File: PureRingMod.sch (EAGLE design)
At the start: 36 parts, among them IC1 TL074P, IC2 TL072P, X1 NC3FD-V

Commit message: added mix control
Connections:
- net GND: now also MICVOL.1, R4.2
- net N$30: no longer R4.2
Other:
- moved on the sheet: R4
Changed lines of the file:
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@@
 <instance part="R2" gate="G$1" x="99.06" y="66.04"/>
 <instance part="R3" gate="G$1" x="-5.08" y="38.1"/>
-<instance part="R4" gate="G$1" x="-5.08" y="66.04"/>
+<instance part="R4" gate="G$1" x="-12.7" y="66.04"/>
 <instance part="R5" gate="G$1" x="132.08" y="63.5"/>
 <instance part="OUTPUT" gate="G$1" x="157.48" y="63.5"/>
@@
 <label x="-35.56" y="88.9" size="1.778" layer="95"/>
 </segment>
+<segment>
+<pinref part="MICVOL" gate="G$1" pin="1"/>
+<pinref part="R4" gate="G$1" pin="2"/>
+<wire x1="-7.62" y1="66.04" x2="-2.54" y2="66.04" width="0.1524" layer="91"/>
+<wire x1="-2.54" y1="66.04" x2="-2.54" y2="83.82" width="0.1524" layer="91"/>
+</segment>
 </net>
 <net name="-12V" class="1">
@@
 <wire x1="121.92" y1="63.5" x2="127" y2="63.5" width="0.1524" layer="91"/>
 <pinref part="R5" gate="G$1" pin="1"/>
-</segment>
-</net>
-<net name="N$13" class="0">
-<segment>
-<pinref part="R4" gate="G$1" pin="1"/>
-<wire x1="-10.16" y1="66.04" x2="-12.7" y2="66.04" width="0.1524" layer="91"/>
-<pinref part="CARRIERAC" gate="G$1" pin="P"/>
-<wire x1="-20.32" y1="66.04" x2="-12.7" y2="66.04" width="0.1524" layer="91"/>
 </segment>
 </net>
@@
 <pinref part="IC1" gate="A" pin="+IN"/>
 <wire x1="7.62" y1="66.04" x2="5.08" y2="66.04" width="0.1524" layer="91"/>
-<pinref part="R4" gate="G$1" pin="2"/>
 <wire x1="5.08" y1="66.04" x2="2.54" y2="66.04" width="0.1524" layer="91"/>
-<wire x1="2.54" y1="66.04" x2="0" y2="66.04" width="0.1524" layer="91"/>
 <wire x1="5.08" y1="88.9" x2="5.08" y2="66.04" width="0.1524" layer="91"/>
 <junction x="5.08" y="66.04"/>
 </segment>
 </net>
+<net name="N$8" class="0">
+<segment>
+<pinref part="CARRIERAC" gate="G$1" pin="P"/>
+<pinref part="R4" gate="G$1" pin="1"/>
+<wire x1="-20.32" y1="66.04" x2="-17.78" y2="66.04" width="0.1524" layer="91"/>
+</segment>
+</net>

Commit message: updated components in feedback circuit of preamp
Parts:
- R12: value 301K -> 330K
- TR1: value 25K -> 10K
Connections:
- net GND: now also OUTPUT.NORM
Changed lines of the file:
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@@
 <part name="R11" library="SparkFun-Resistors" deviceset="330OHM" device="-HORIZ-1/10W-5%" value="316K"/>
 <part name="C5" library="SparkFun-Capacitors" deviceset="0.1UF" device="-KIT-EZ-50V-20%" value="4u7f"/>
-<part name="R12" library="SparkFun-Resistors" deviceset="330OHM" device="-HORIZ-1/10W-5%" value="301K"/>
+<part name="R12" library="SparkFun-Resistors" deviceset="330OHM" device="-HORIZ-1/10W-5%" value="330K"/>
 <part name="R13" library="SparkFun-Resistors" deviceset="330OHM" device="-HORIZ-1/10W-5%" value="10K"/>
 <part name="R14" library="SparkFun-Resistors" deviceset="330OHM" device="-HORIZ-1/10W-5%" value="100"/>
-<part name="TR1" library="INSTRUO" deviceset="TRIMMER_TH3" device="" value="25K"/>
+<part name="TR1" library="INSTRUO" deviceset="TRIMMER_TH3" device="" value="10K"/>
 <part name="MICVOL" library="GMSN" deviceset="9MMPOT" device=""/>
 </parts>
@@
 <wire x1="149.86" y1="60.96" x2="149.86" y2="58.42" width="0.1524" layer="91"/>
 <label x="149.86" y="55.88" size="1.778" layer="95"/>
+<pinref part="OUTPUT" gate="G$1" pin="NORM"/>
+<wire x1="152.4" y1="63.5" x2="149.86" y2="63.5" width="0.1524" layer="91"/>
+<wire x1="149.86" y1="63.5" x2="149.86" y2="60.96" width="0.1524" layer="91"/>
+<junction x="149.86" y="60.96"/>
 </segment>
 <segment>

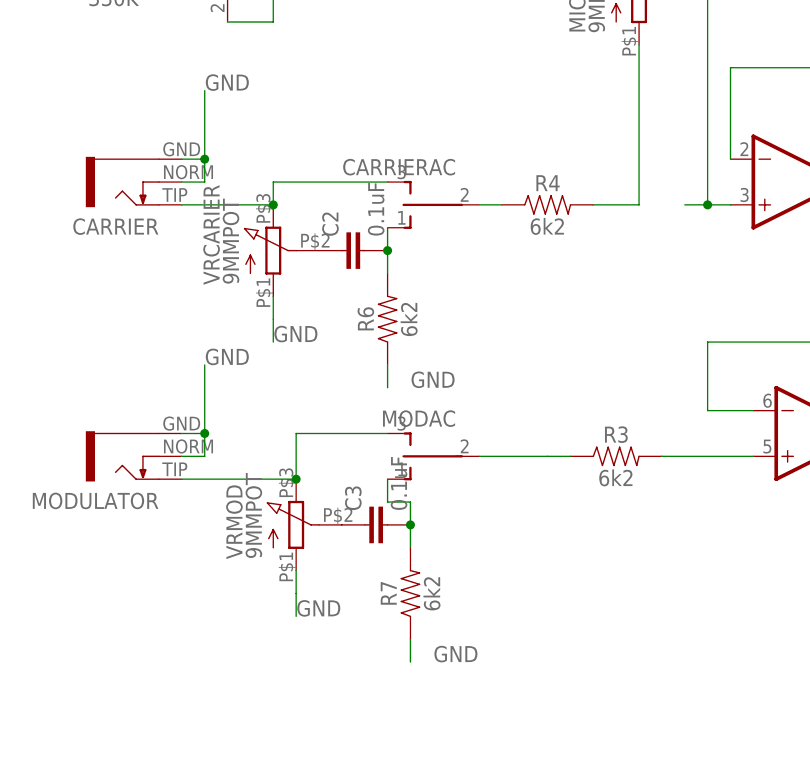
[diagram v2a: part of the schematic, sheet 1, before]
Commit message: Corrected values on input circuit
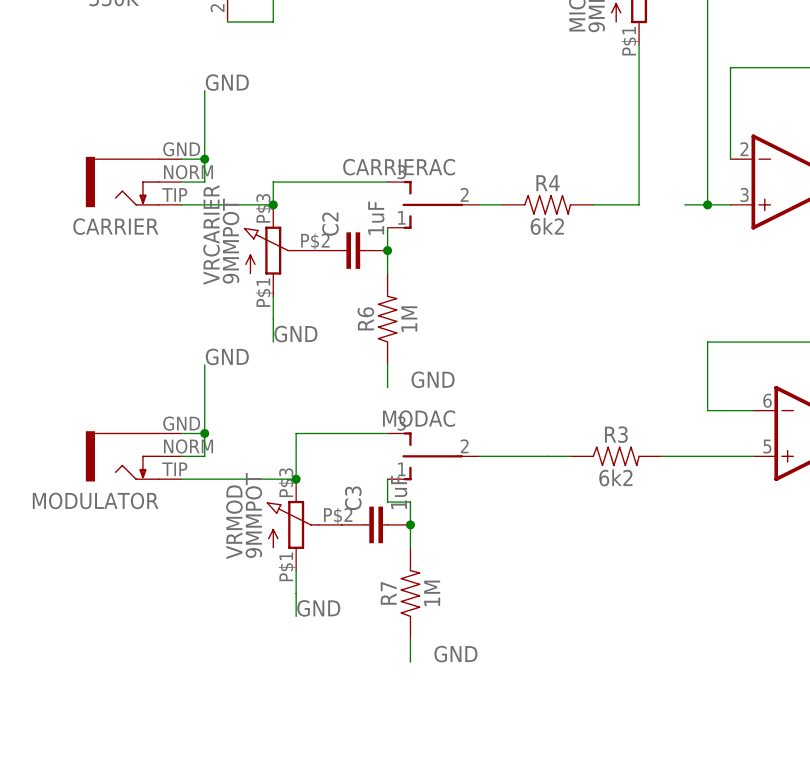
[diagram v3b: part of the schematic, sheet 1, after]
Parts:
- C2, C3: value 0.1uF -> 1uF
- R6, R7: value 6k2 -> 1M
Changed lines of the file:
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@@
 <part name="VRCARIER" library="GMSN" deviceset="9MMPOT" device=""/>
 <part name="VRMOD" library="GMSN" deviceset="9MMPOT" device=""/>
-<part name="C2" library="SparkFun-Capacitors" deviceset="0.1UF" device="-KIT-EZ-50V-20%" value="0.1uF"/>
-<part name="C3" library="SparkFun-Capacitors" deviceset="0.1UF" device="-KIT-EZ-50V-20%" value="0.1uF"/>
-<part name="R6" library="SparkFun-Resistors" deviceset="330OHM" device="-HORIZ-1/10W-5%" value="6k2"/>
-<part name="R7" library="SparkFun-Resistors" deviceset="330OHM" device="-HORIZ-1/10W-5%" value="6k2"/>
+<part name="C2" library="SparkFun-Capacitors" deviceset="0.1UF" device="-KIT-EZ-50V-20%" value="1uF"/>
+<part name="C3" library="SparkFun-Capacitors" deviceset="0.1UF" device="-KIT-EZ-50V-20%" value="1uF"/>
+<part name="R6" library="SparkFun-Resistors" deviceset="330OHM" device="-HORIZ-1/10W-5%" value="1M"/>
+<part name="R7" library="SparkFun-Resistors" deviceset="330OHM" device="-HORIZ-1/10W-5%" value="1M"/>
 <part name="X1" library="con-neutrik_ag" library_urn="urn:adsk.eagle:library:166" deviceset="NC3" device="FD-V" package3d_urn="urn:adsk.eagle:package:8819/1">
 <attribute name="RS-PART" value="448-244"/>

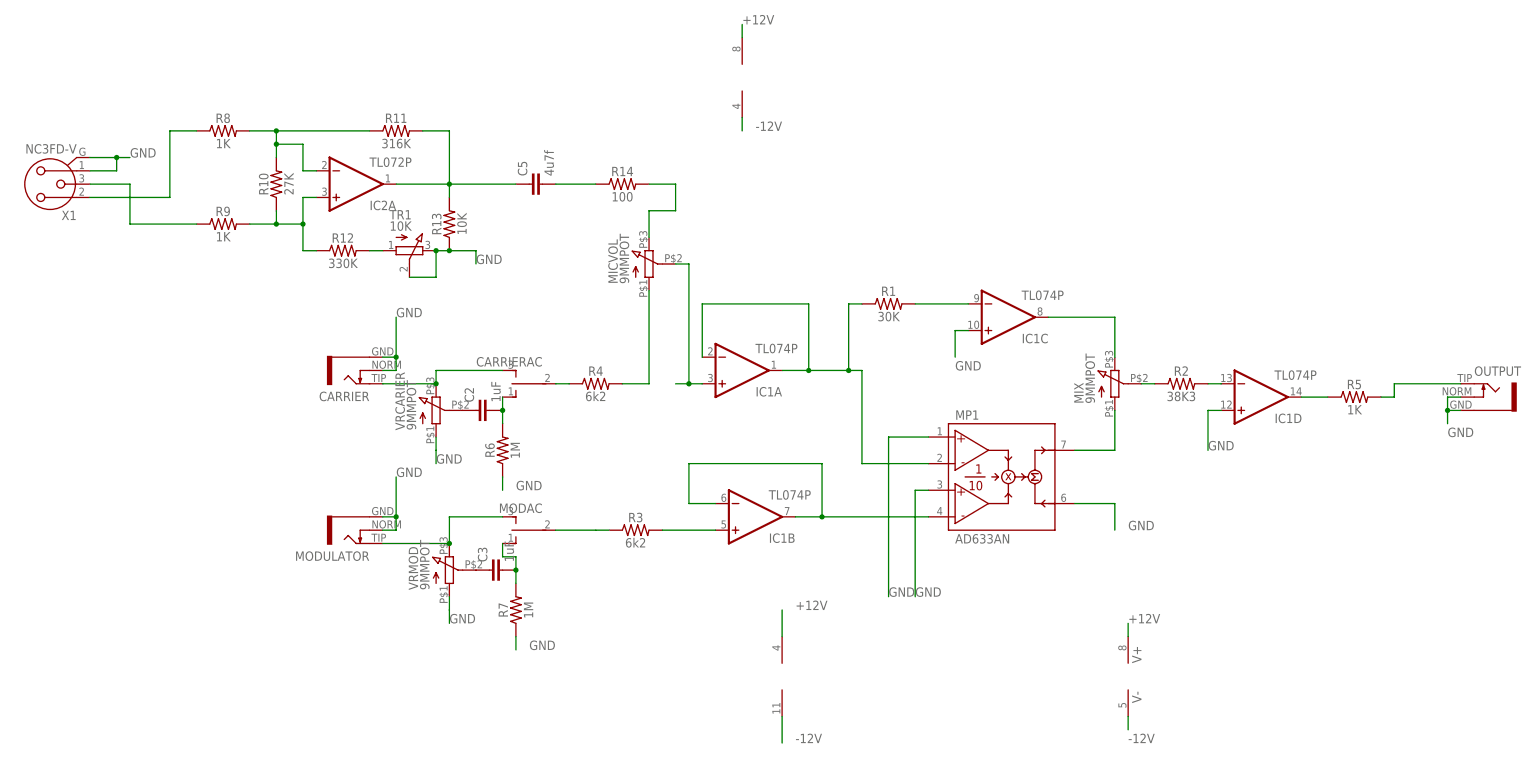
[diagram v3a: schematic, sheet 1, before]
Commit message: corrected input components
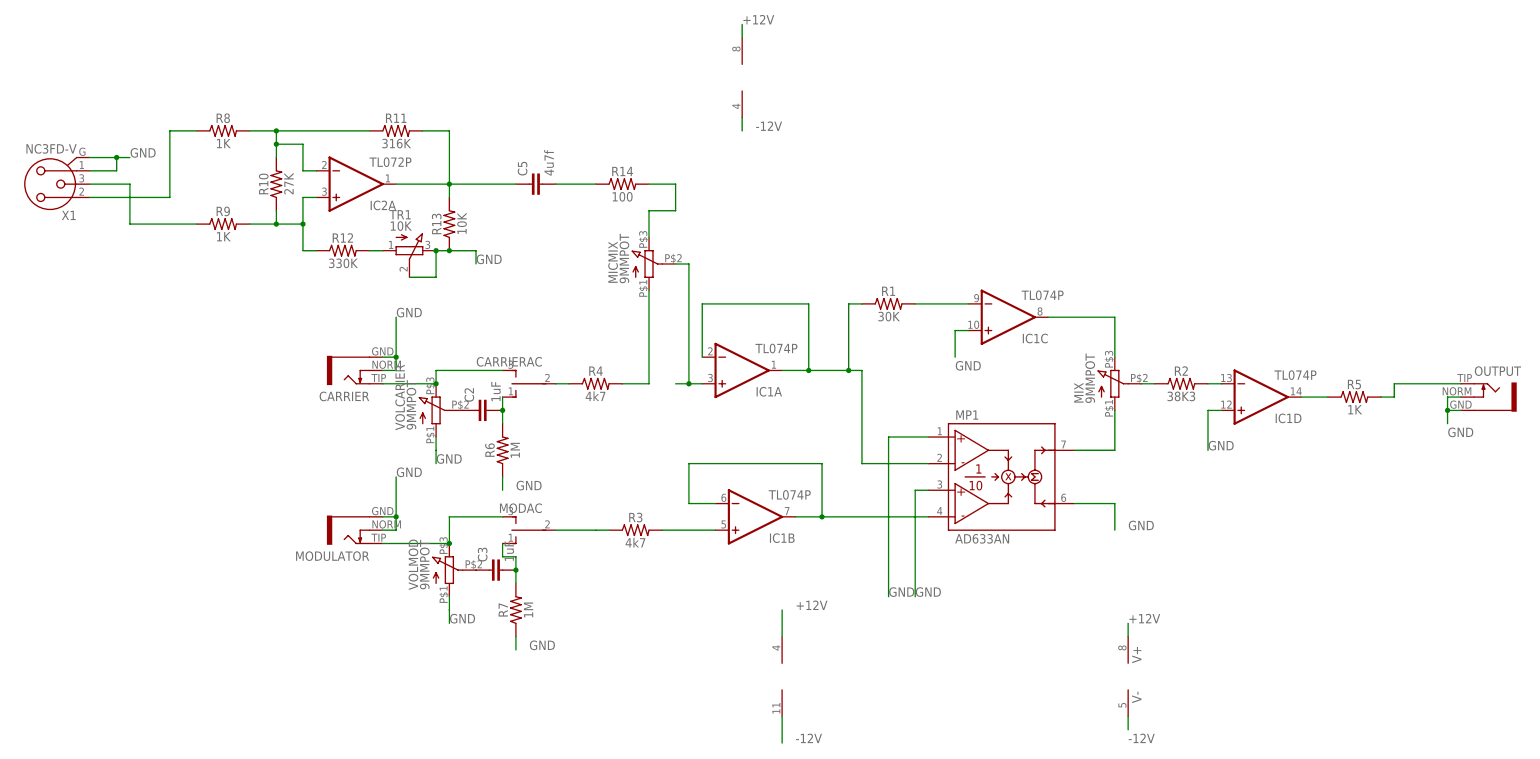
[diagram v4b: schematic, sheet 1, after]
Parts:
- R3, R4: value 6k2 -> 4k7
- renumbered MICVOL to MICMIX, VRCARIER to VOLCARIER, VRMOD to VOLMOD

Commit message: added missing parts
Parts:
- added R15: 10K, SparkFun-Resistors:330OHM-HORIZ-1/10W-5%
- added R16: 27K, SparkFun-Resistors:330OHM-HORIZ-1/10W-5%
- R1: value 30K -> 20K
- R2: value 38K3 -> 27K
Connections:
- net N$12: now also R16.2
- net N$4: now also R15.2
- net N$5: now also R15.1
- net N$7: now also R16.1
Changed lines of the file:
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@@
 <part name="POWER" library="SparkFun-Connectors" deviceset="M05X2" device="SHD"/>
 <part name="MIX" library="GMSN" deviceset="9MMPOT" device=""/>
-<part name="R1" library="SparkFun-Resistors" deviceset="330OHM" device="-HORIZ-1/10W-5%" value="30K"/>
-<part name="R2" library="SparkFun-Resistors" deviceset="330OHM" device="-HORIZ-1/10W-5%" value="38K3"/>
+<part name="R1" library="SparkFun-Resistors" deviceset="330OHM" device="-HORIZ-1/10W-5%" value="20K"/>
+<part name="R2" library="SparkFun-Resistors" deviceset="330OHM" device="-HORIZ-1/10W-5%" value="27K"/>
 <part name="C4" library="SparkFun-Capacitors" deviceset="10UF-POLAR" device="-RADIAL-2.5MM-25V-20%" value="10uF"/>
 <part name="C1" library="SparkFun-Capacitors" deviceset="10UF-POLAR" device="-RADIAL-2.5MM-25V-20%" value="10uF"/>
@@
 <part name="TR1" library="INSTRUO" deviceset="TRIMMER_TH3" device="" value="10K"/>
 <part name="MICMIX" library="GMSN" deviceset="9MMPOT" device=""/>
+<part name="R15" library="SparkFun-Resistors" deviceset="330OHM" device="-HORIZ-1/10W-5%" value="10K"/>
+<part name="R16" library="SparkFun-Resistors" deviceset="330OHM" device="-HORIZ-1/10W-5%" value="27K"/>
 </parts>
 <sheets>
@@
 </instance>
 <instance part="IC2" gate="P" x="15.24" y="124.46"/>
+<instance part="R15" gate="G$1" x="68.58" y="91.44">
+<attribute name="NAME" x="68.58" y="92.964" size="1.778" layer="95" font="vector" align="bottom-center"/>
+<attribute name="VALUE" x="68.58" y="89.916" size="1.778" layer="96" font="vector" align="top-center"/>
+</instance>
+<instance part="R16" gate="G$1" x="114.3" y="78.74">
+<attribute name="NAME" x="114.3" y="80.264" size="1.778" layer="95" font="vector" align="bottom-center"/>
+<attribute name="VALUE" x="114.3" y="77.216" size="1.778" layer="96" font="vector" align="top-center"/>
+</instance>
 </instances>
 <busses>
@@
 <segment>
 <pinref part="IC1" gate="C" pin="OUT"/>
-<wire x1="73.66" y1="78.74" x2="86.36" y2="78.74" width="0.1524" layer="91"/>
+<wire x1="73.66" y1="78.74" x2="78.74" y2="78.74" width="0.1524" layer="91"/>
 <pinref part="MIX" gate="G$1" pin="3"/>
+<wire x1="78.74" y1="78.74" x2="86.36" y2="78.74" width="0.1524" layer="91"/>
 <wire x1="86.36" y1="78.74" x2="86.36" y2="71.12" width="0.1524" layer="91"/>
+<wire x1="78.74" y1="78.74" x2="78.74" y2="91.44" width="0.1524" layer="91"/>
+<wire x1="78.74" y1="91.44" x2="73.66" y2="91.44" width="0.1524" layer="91"/>
+<pinref part="R15" gate="G$1" pin="2"/>
 </segment>
 </net>
@@
 <pinref part="R1" gate="G$1" pin="2"/>
 <pinref part="IC1" gate="C" pin="-IN"/>
-<wire x1="48.26" y1="81.28" x2="58.42" y2="81.28" width="0.1524" layer="91"/>
+<wire x1="48.26" y1="81.28" x2="53.34" y2="81.28" width="0.1524" layer="91"/>
+<wire x1="53.34" y1="81.28" x2="58.42" y2="81.28" width="0.1524" layer="91"/>
+<wire x1="53.34" y1="91.44" x2="53.34" y2="81.28" width="0.1524" layer="91"/>
+<junction x="53.34" y="81.28"/>
+<wire x1="53.34" y1="91.44" x2="63.5" y2="91.44" width="0.1524" layer="91"/>
+<pinref part="R15" gate="G$1" pin="1"/>
 </segment>
 </net>
@@
 <pinref part="IC1" gate="D" pin="-IN"/>
 <wire x1="104.14" y1="66.04" x2="106.68" y2="66.04" width="0.1524" layer="91"/>
+<wire x1="104.14" y1="66.04" x2="104.14" y2="78.74" width="0.1524" layer="91"/>
+<junction x="104.14" y="66.04"/>
+<pinref part="R16" gate="G$1" pin="1"/>
+<wire x1="104.14" y1="78.74" x2="109.22" y2="78.74" width="0.1524" layer="91"/>
 </segment>
 </net>
@@
 <segment>
 <pinref part="IC1" gate="D" pin="OUT"/>
-<wire x1="121.92" y1="63.5" x2="127" y2="63.5" width="0.1524" layer="91"/>
+<wire x1="121.92" y1="63.5" x2="124.46" y2="63.5" width="0.1524" layer="91"/>
 <pinref part="R5" gate="G$1" pin="1"/>
-</segment>
-</net>
+<wire x1="124.46" y1="63.5" x2="127" y2="63.5" width="0.1524" layer="91"/>
+<wire x1="124.46" y1="63.5" x2="124.46" y2="78.74" width="0.1524" layer="91"/>
+<junction x="124.46" y="63.5"/>
+<pinref part="R16" gate="G$1" pin="2"/>
+<wire x1="119.38" y1="78.74" x2="124.46" y2="78.74" width="0.1524" layer="91"/>
+</segment>
+</net>

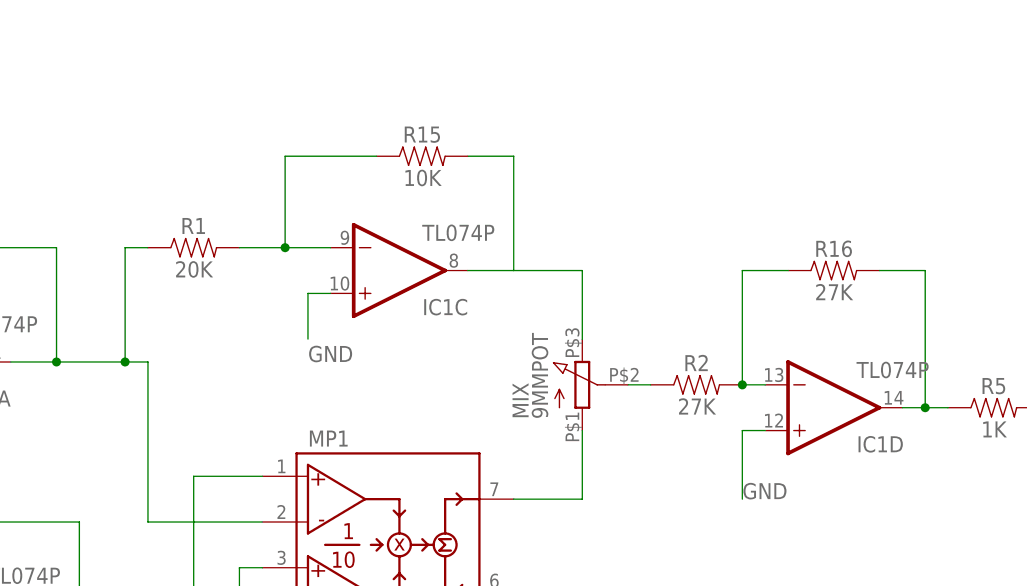
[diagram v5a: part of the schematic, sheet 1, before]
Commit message: Changed output circuit values
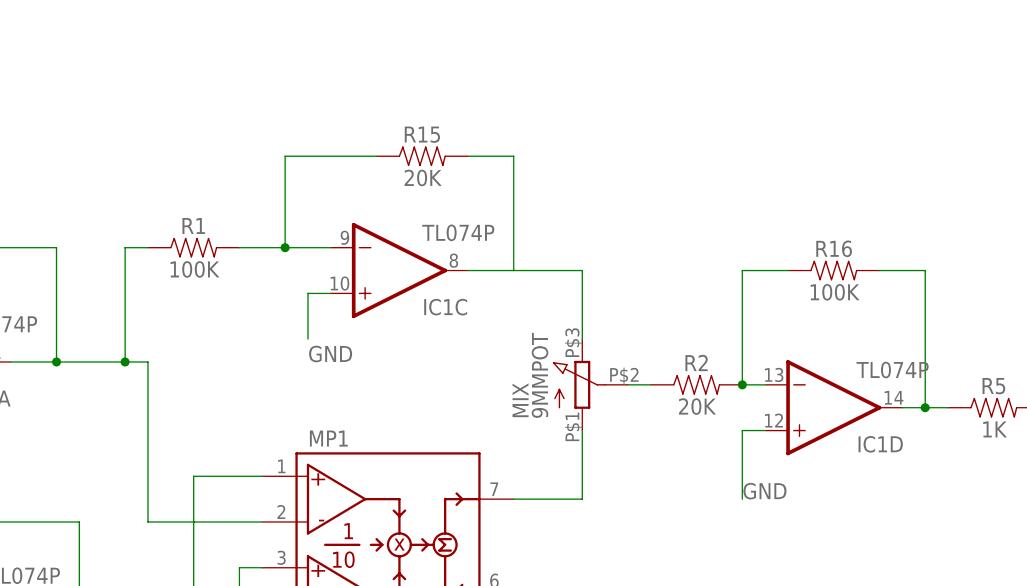
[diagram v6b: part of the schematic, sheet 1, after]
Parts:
- R1: value 20K -> 100K
- R15: value 10K -> 20K
- R16: value 27K -> 100K
- R2: value 27K -> 20K
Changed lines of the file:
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@@
 <part name="POWER" library="SparkFun-Connectors" deviceset="M05X2" device="SHD"/>
 <part name="MIX" library="GMSN" deviceset="9MMPOT" device=""/>
-<part name="R1" library="SparkFun-Resistors" deviceset="330OHM" device="-HORIZ-1/10W-5%" value="20K"/>
-<part name="R2" library="SparkFun-Resistors" deviceset="330OHM" device="-HORIZ-1/10W-5%" value="27K"/>
+<part name="R1" library="SparkFun-Resistors" deviceset="330OHM" device="-HORIZ-1/10W-5%" value="100K"/>
+<part name="R2" library="SparkFun-Resistors" deviceset="330OHM" device="-HORIZ-1/10W-5%" value="20K"/>
 <part name="C4" library="SparkFun-Capacitors" deviceset="10UF-POLAR" device="-RADIAL-2.5MM-25V-20%" value="10uF"/>
 <part name="C1" library="SparkFun-Capacitors" deviceset="10UF-POLAR" device="-RADIAL-2.5MM-25V-20%" value="10uF"/>
@@
 <part name="TR1" library="INSTRUO" deviceset="TRIMMER_TH3" device="" value="10K"/>
 <part name="MICMIX" library="GMSN" deviceset="9MMPOT" device=""/>
-<part name="R15" library="SparkFun-Resistors" deviceset="330OHM" device="-HORIZ-1/10W-5%" value="10K"/>
-<part name="R16" library="SparkFun-Resistors" deviceset="330OHM" device="-HORIZ-1/10W-5%" value="27K"/>
+<part name="R15" library="SparkFun-Resistors" deviceset="330OHM" device="-HORIZ-1/10W-5%" value="20K"/>
+<part name="R16" library="SparkFun-Resistors" deviceset="330OHM" device="-HORIZ-1/10W-5%" value="100K"/>
 </parts>
 <sheets>

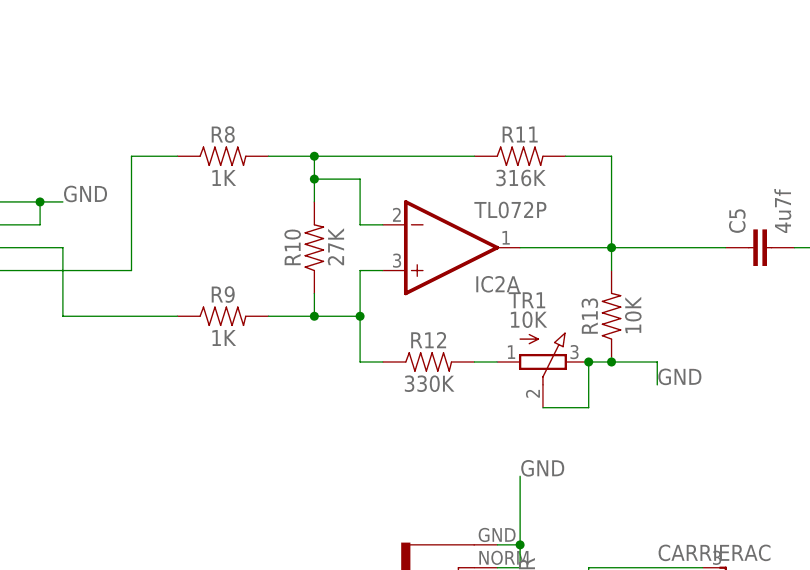
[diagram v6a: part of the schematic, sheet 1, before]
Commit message: modified input mic circuit
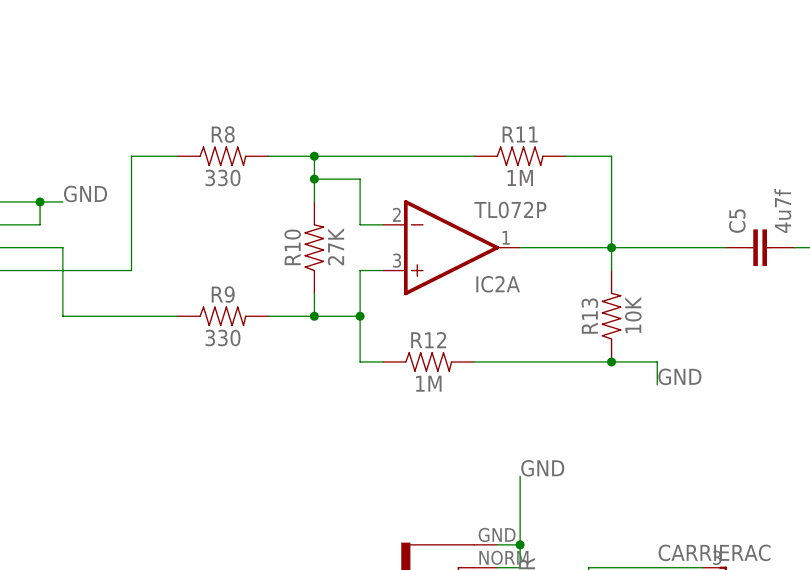
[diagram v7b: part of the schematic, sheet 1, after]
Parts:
- removed TR1: 10K, INSTRUO:TRIMMER_TH3
- R11: value 316K -> 1M
- R12: value 330K -> 1M
- R8, R9: value 1K -> 330
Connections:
- removed net N$28: R12.2, TR1.1
- net GND: now also R12.2; no longer TR1.2, TR1.3

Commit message: Fixed input
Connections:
- net N$16: no longer CARRIERAC.S
- net N$17: no longer MODAC.S
- net N$18: now also CARRIERAC.S
- net N$19: now also MODAC.S
